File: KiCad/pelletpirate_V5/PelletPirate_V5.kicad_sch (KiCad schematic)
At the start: 130 parts, among them J1 SJ1-3523NG_Jack_PP, J2 SJ1-3523NG_Jack_PP, J3 SJ1-3523NG_Jack_PP, J4 SJ1-3523NG_Jack_PP, J5 SJ1-3523NG_Jack_PP, J6 Conn_01x04, J7 Conn_01x04_Socket, J8 USB4145-03-0170-C, J9 TB002-500-02BE, T1 BTA12-600BWRG, T2 BTA12-600BWRG, T3 BTA12-600BWRG, U1 USBLC6-2SC6, U3 H11AA1M

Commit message: V5 post-cancel fixes: C9 0402, C43 VBUS ballast, C39/C40 boot pair, R20 0805
Order cancelled 2026-08-28; V5 is the active design again. Fixes since:
- C9: footprint corrected to 0402, MPN C0402C104K3RACTU (package now matches part)
- C43 NEW: 100nF 0402 at U1 pin 5, /VBUS->GND ESD ballast (verified 1.63mm from pin)
- C39: EN cap 0.1uF -> 1.0uF 25V KEMET C0603C105K3RACTU (0603 X7R) per Espressif
- C40: IO0 debounce cap rewired +3.3V -> GND (orthodox; linked with C39 change,
  EN delay 10ms >> IO0 rise 1ms, boot-strap race eliminated)
- R20: MPN corrected to RC0805FR-0710KL, footprint normalized to plain 0805
Audits passed on this state: ESP32 pin-by-pin (zero notes), MAX1-5 tiles,
H11AA1/MOC3053, J8/U1 USB, full board-symbol-footprint-BOM reconciliation
(118 refs, 70 package-decoded lines, 0 errors). ERC 0 / DRC 0 / parity 0.

Co-Authored-By: Claude Fable 5 <noreply@anthropic.com>
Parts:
- added C43: 0.1µF 25V, Capacitor_SMD:C_0402_1005Metric, symbol Device:C
- C39: value 0.1µF 25V -> 1.0µF 25V; footprint Capacitor_SMD:C_0402_1005Metric -> Capacitor_SMD:C_0603_1608Metric; LINK https://www.digikey.com/en/products/detail/kemet/C0402C104K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 -> https://www.digikey.com/en/products/detail/kemet/C0603C105K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; MP C0402C104K3RACTU -> C0603C105K3RACTU
- C9: footprint Capacitor_SMD:C_0805_2012Metric -> Capacitor_SMD:C_0402_1005Metric
- R20: footprint Resistor_SMD:R_0805_2012Metric_Pad1.20x1.40mm_HandSolder -> Resistor_SMD:R_0805_2012Metric; LINK https://www.digikey.com/en/products/detail/yageo/RC0402FR-0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 -> https://www.digikey.com/en/products/detail/yageo/RC0805FR-0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; MP RC0402FR-0710KL -> RC0805FR-0710KL
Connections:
- net +3.3V: no longer C40.2
- net GND: now also C40.2, C43.2
- net VBUS: now also C43.1
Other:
- moved on the sheet: C40, C42, R41, R42, R43, TP1, TP2, U3

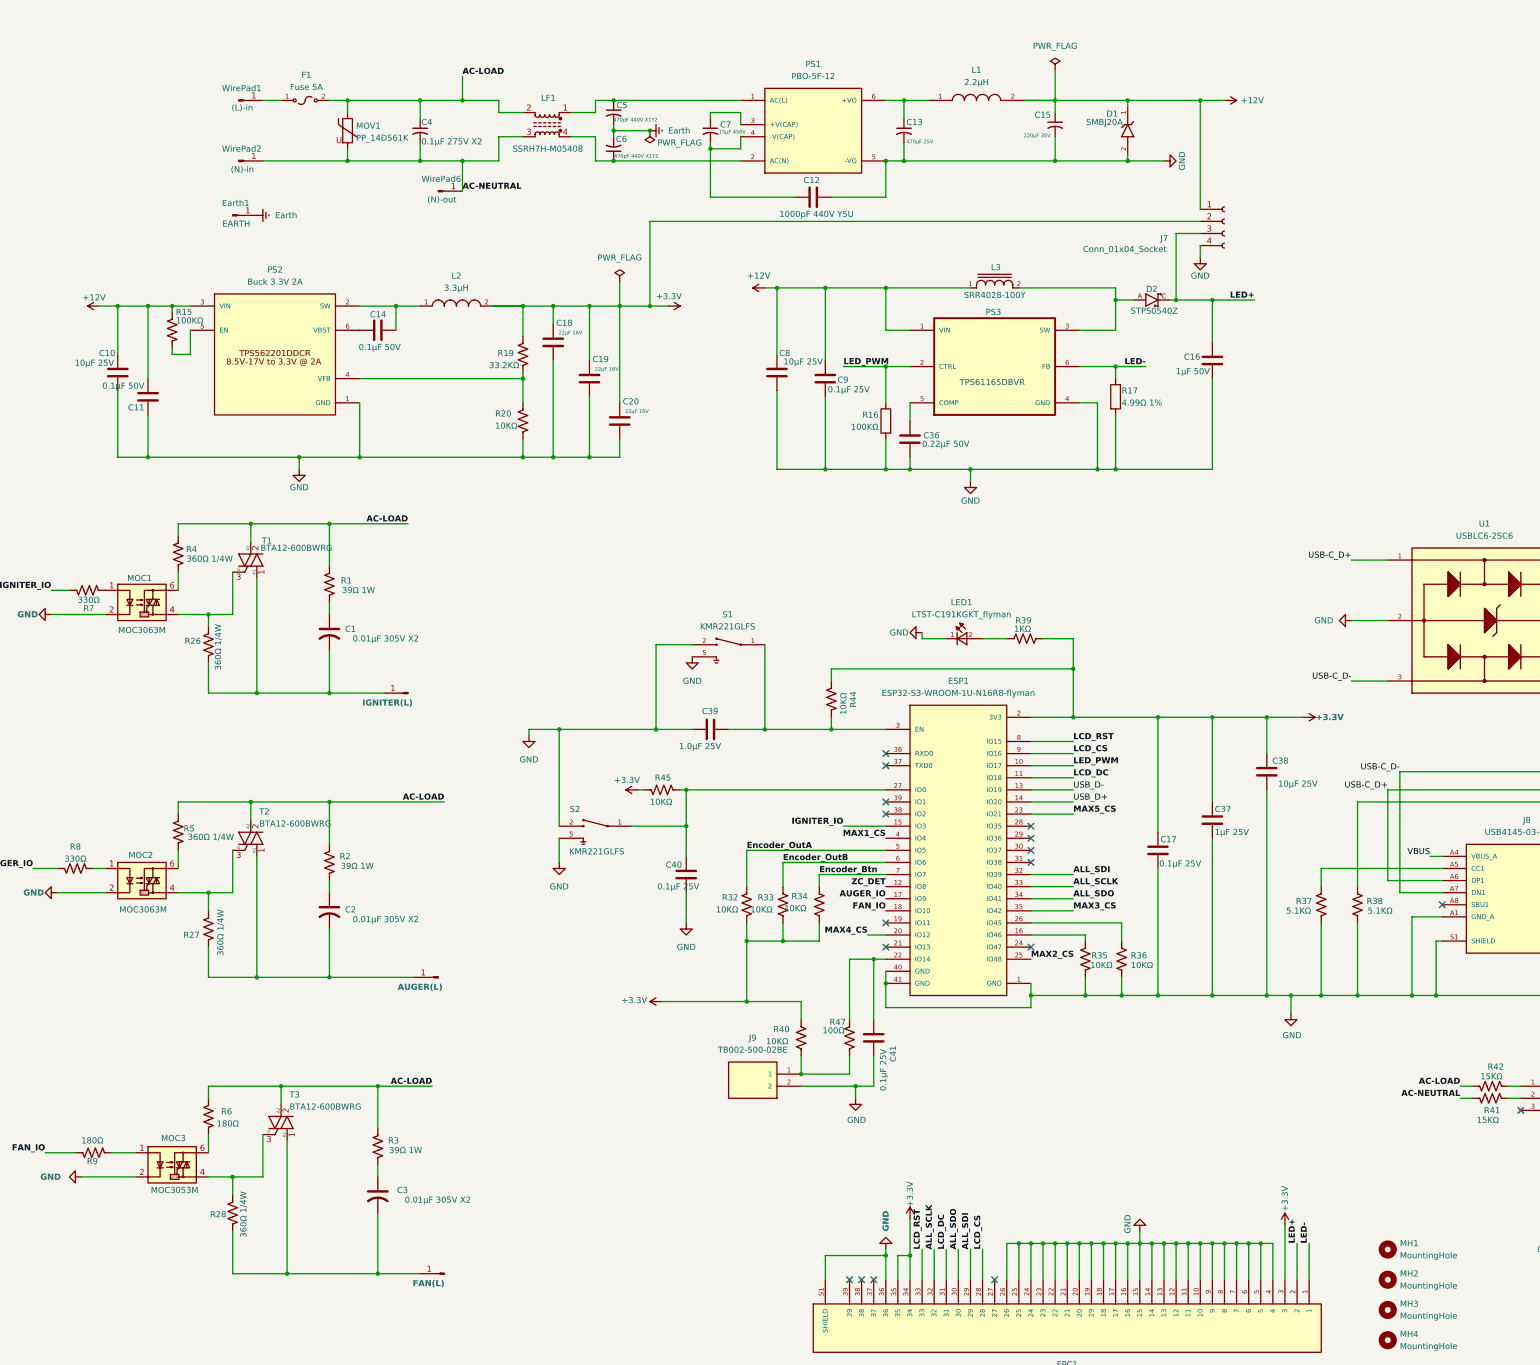
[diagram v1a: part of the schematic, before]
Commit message: V5 raft complete: 4 work packages + C48 damping bulk, all audited, ERC/DRC/netclass clean
WP1: C44/C45 22uF at ESP (raft bulk). WP2: 33R series R at SPI driver pads (R48-51,
stubs <2.2mm). WP3: FL1 bead + C46/C47 panel island (/3V3_LCD, FPC-only membership).
WP4: L5 HF bead after Fig-2 network (D1/C15 upstream preserved) + C48 220uF damping
bulk (resonance 50k->12kHz, Q~1). Netclass patterns added for /3V3_LCD + Net-(C15-Pad1).
EE-soundness review: resonances quantified, Middlebrook margin 80x, timing budgets clear.
Acceptance: runt sentinel 0/min on AC at first article.

Co-Authored-By: Claude Fable 5 <noreply@anthropic.com>
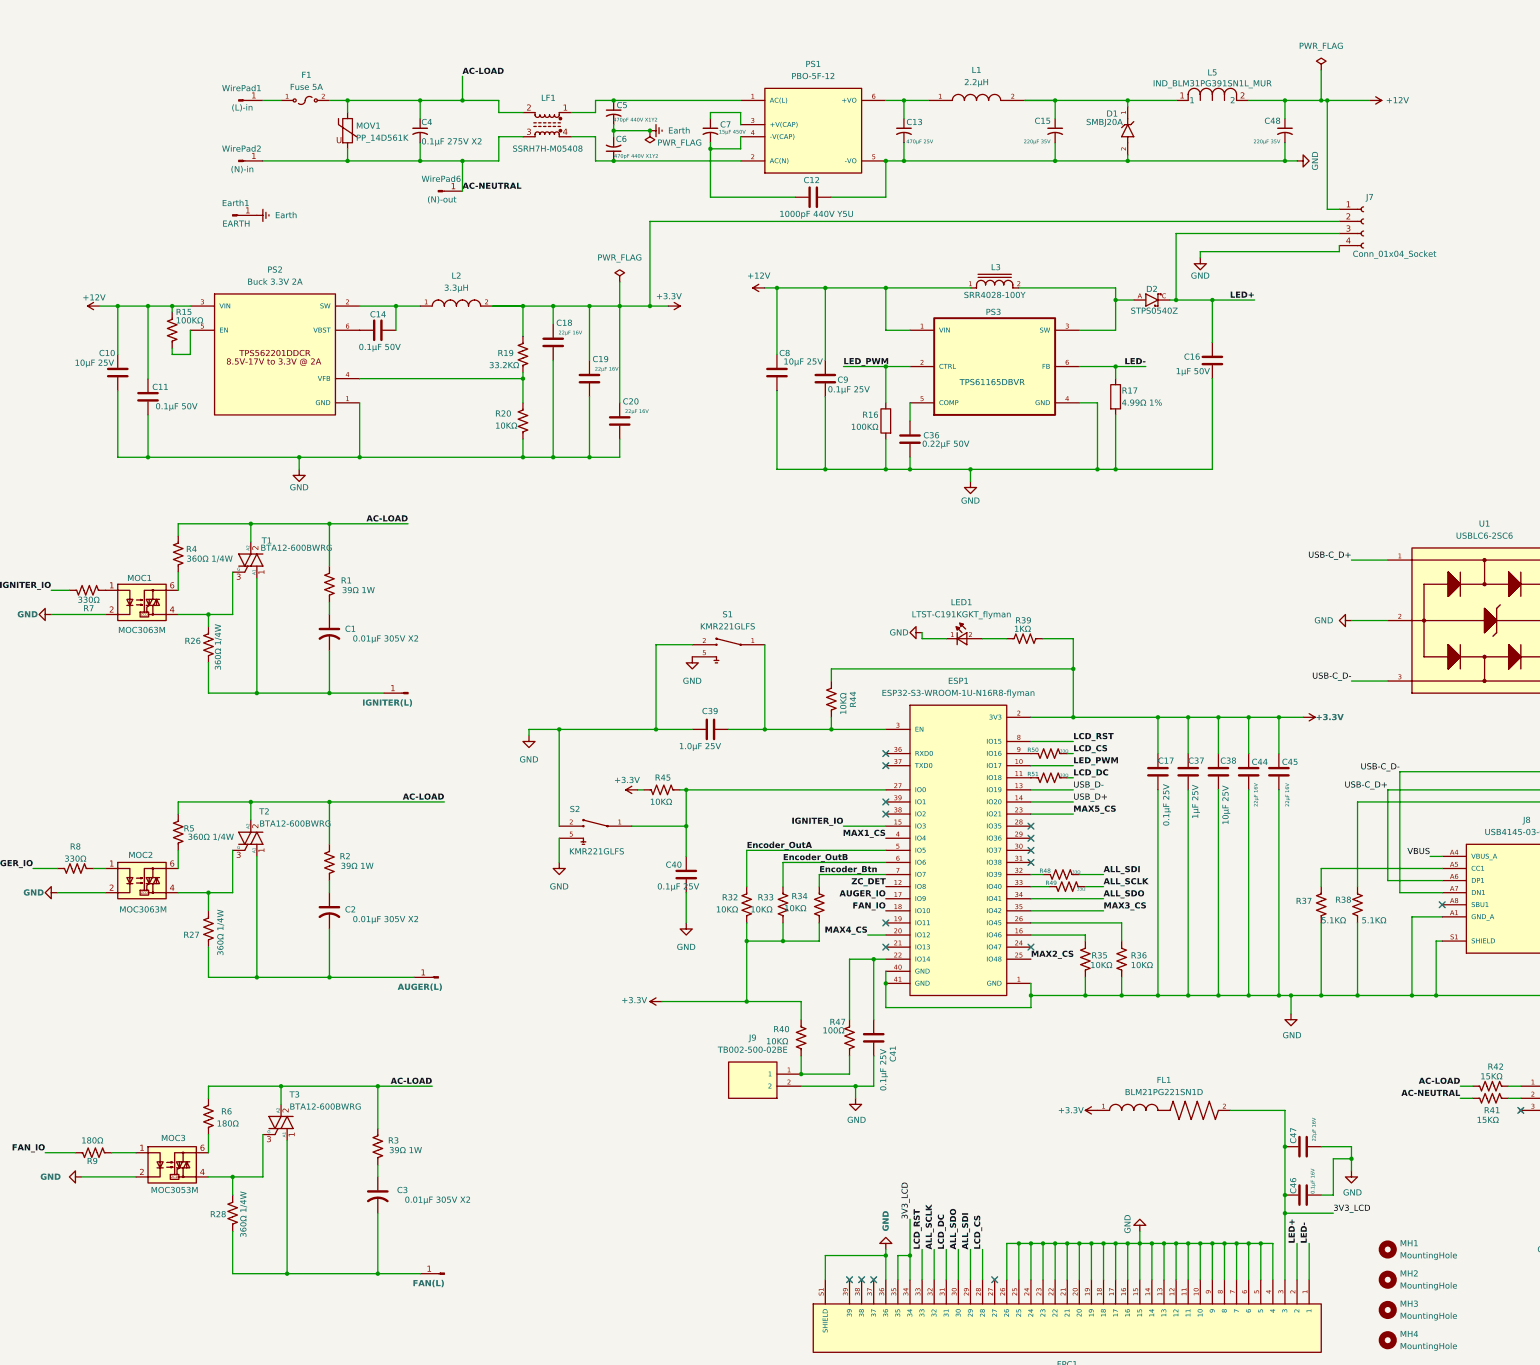
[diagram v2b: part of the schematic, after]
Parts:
- added C44, C45, C47: 22µF 16V, Capacitor_SMD:C_1206_3216Metric, symbol Device:C
- added C46: 0.1µF 16V, Capacitor_SMD:C_0402_1005Metric, symbol Device:C
- added C48: 220µF 35V, Capacitor_THT:CP_Radial_D8.0mm_P3.50mm, symbol Device:C_Small_US
- added FL1: BLM21PG221SN1D, Ferrite_Bead:BEADC2012X105N, symbol BLM21PG221SN1D:BLM21PG221SN1D
- added L5: IND_BLM31PG391SN1L_MUR, Ferrite_Bead_12V:IND_BLM31PG391SN1L_MUR, symbol IND_BLM31PG391SN1L_MUR:IND_BLM31PG391SN1L_MUR
- added R48, R49, R50, R51: 33Ω, Resistor_SMD:R_0402_1005Metric, symbol Device:R_US
- C38: LINK https://www.digikey.com/en/products/detail/kemet/C1206C106K3RACTU/3317648 -> https://www.digikey.com/en/products/detail/kemet/C1206C106K3RACTU/3317648; MP C1206C106K3RACTU -> C1206C106K3RACTU
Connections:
- net +12V: now also C48.1, L5.2; no longer C15.1, D1.1, L1.2
- net +3.3V: now also C44.1, C45.1, FL1.1; no longer FPC1.3, FPC1.34, FPC1.35
- net ALL_SCLK: now also R49.2; no longer ESP1.33 (IO40)
- net ALL_SDI: now also R48.2; no longer ESP1.32 (IO39)
- net GND: now also C44.2, C45.2, C46.1, C47.2, C48.2
- net LCD_CS: now also R50.2; no longer ESP1.9 (IO16)
- net LCD_DC: now also R51.2; no longer ESP1.11 (IO18)
- new net: C15.1, D1.1, L1.2, L5.1
- new net: ESP1.11 (IO18), R51.1
- new net: ESP1.32 (IO39), R48.1
- new net: ESP1.33 (IO40), R49.1
- new net: ESP1.9 (IO16), R50.1
- new net 3V3_LCD: C46.2, C47.1, FL1.2, FPC1.3, FPC1.34, FPC1.35
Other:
- moved on the sheet: C15, C17, C37, C38, J7

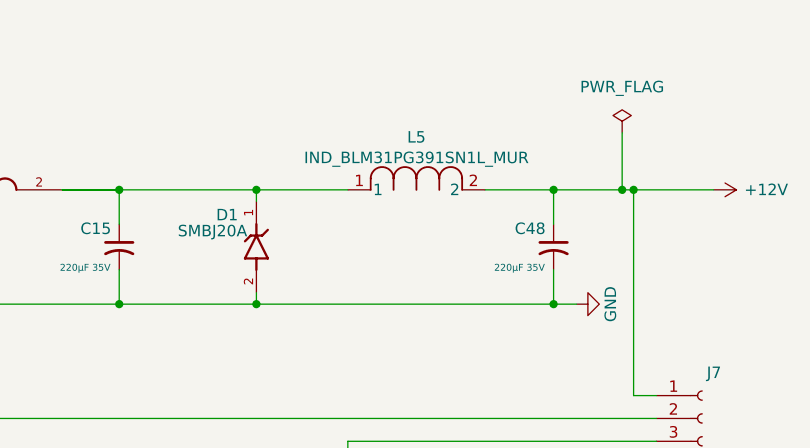
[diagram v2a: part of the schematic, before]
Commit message: V5 PCBWay package regenerated: raft revision, 61 lines / 129 components, 19 no-sub lines
Gerbers+drill (25 slots), positions (148), BOM with FL1/L5/C13/C15+C48 no-sub additions,
assembly notes updated (J9 orientation, C48 polarity, supersedes cancelled 08-27 upload).
Old package archived to archive_to_delete/. L5 601 value+footprint+3D model settled.
J9 flipped: entry faces west edge. Final ERC/DRC 0/0, parity 142/142.

Co-Authored-By: Claude Fable 5 <noreply@anthropic.com>
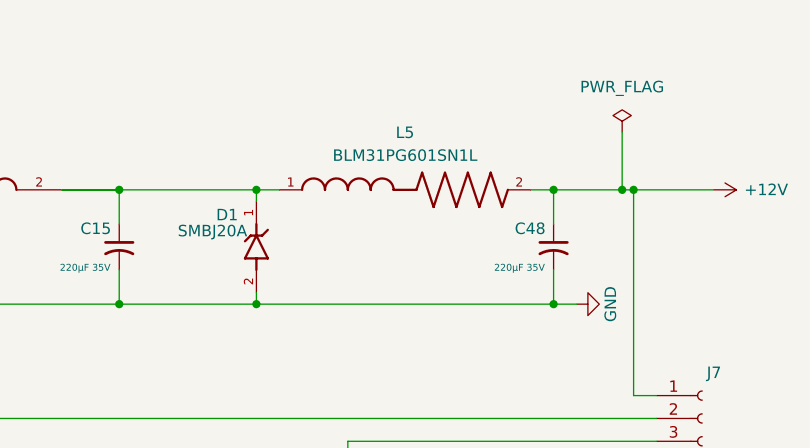
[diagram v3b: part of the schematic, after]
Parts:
- removed L5: IND_BLM31PG391SN1L_MUR, Ferrite_Bead_12V:IND_BLM31PG391SN1L_MUR, symbol IND_BLM31PG391SN1L_MUR:IND_BLM31PG391SN1L_MUR
- added L5: BLM31PG601SN1L, Ferrite_Bead_12V_Flyman:BEADC3216X130N_flyman, symbol BLM31PG601SN1L_flyman:BLM31PG601SN1L
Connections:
- net +12V: now also L5.2
- net at C15.1, D1.1, L1.2: now also L5.1
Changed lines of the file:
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@@
 	)
 	(junction
-		(at 283.21 34.29)
+		(at 452.12 129.54)
 		(diameter 0)
 		(color 0 0 0 0)
 	)
 	(junction
-		(at 452.12 129.54)
+		(at 265.43 274.32)
 		(diameter 0)
 		(color 0 0 0 0)
 	)
 	(junction
-		(at 265.43 274.32)
+		(at 283.21 34.29)
 		(diameter 0)
 		(color 0 0 0 0)
@@
 	(wire
 		(pts
-			(xy 275.59 34.29) (xy 283.21 34.29)
+			(xy 280.67 34.29) (xy 283.21 34.29)
 		)
 		(stroke
@@
 	(wire
 		(pts
-			(xy 250.19 34.29) (xy 260.35 34.29)
+			(xy 250.19 34.29) (xy 252.73 34.29)
 		)
 		(stroke
@@
 	)
 	(symbol
+		(lib_id "BLM31PG601SN1L_flyman:BLM31PG601SN1L")
+		(at 267.97 34.29 0)
+		(unit 1)
+		(body_style 1)
+		(exclude_from_sim no)
+		(in_bom yes)
+		(on_board yes)
+		(in_pos_files yes)
+		(dnp no)
+		(fields_autoplaced yes)
+		(property "Reference" "L5"
+			(at 266.7 27.94 0)
+			(show_name no)
+			(do_not_autoplace no)
+			(effects
+				(font
+					(size 1.27 1.27)
+				)
+			)
+		)
+		(property "Value" "BLM31PG601SN1L"
+			(at 266.7 30.48 0)
+			(show_name no)
+			(do_not_autoplace no)
+			(effects
+				(font
+					(size 1.27 1.27)
+				)
+			)
+		)
+		(property "Footprint" "Ferrite_Bead_12V_Flyman:BEADC3216X130N_flyman"
+			(at 267.97 34.29 0)
+			(hide yes)
+			(show_name no)
+			(do_not_autoplace no)
+			(effects
+				(font
+					(size 1.27 1.27)
+				)
+				(justify bottom)
+			)
+		)
+		(property "Datasheet" ""
+			(at 267.97 34.29 0)
+			(hide yes)
+			(show_name no)
+			(do_not_autoplace no)
+			(effects
+				(font
+					(size 1.27 1.27)
+				)
+			)
+		)
+		(property "Description" "600 Ohms @ 100 MHz 1 Power Line Ferrite Bead 1206 (3216 Metric) 1.5A 80mOhm"
+			(at 267.97 34.29 0)
+			(hide yes)
+			(show_name no)
+			(do_not_autoplace no)
+			(effects
+				(font
+					(size 1.27 1.27)
+				)
+				(justify bottom)
+			)
+		)
+		(property "MF" "Murata"
+			(at 267.97 34.29 0)
+			(hide yes)
+			(show_name no)
+			(do_not_autoplace no)
+			(effects
+				(font
+					(size 1.27 1.27)
+				)
+				(justify bottom)
+			)
+		)
+		(property "Package" "3216 Murata"
+			(at 267.97 34.29 0)
+			(hide yes)
+			(show_name no)
+			(do_not_autoplace no)
+			(effects
+				(font
+					(size 1.27 1.27)
+				)
+				(justify bottom)
+			)
+		)
+		(property "Price" "None"
+			(at 267.97 34.29 0)
+			(hide yes)
+			(show_name no)
+			(do_not_autoplace no)
+			(effects
+				(font
+					(size 1.27 1.27)
+				)
+				(justify bottom)
+			)
+		)
+		(property "SnapEDA_Link" "https://www.snapeda.com/parts/BLM31PG601SN1L/Murata/view-part/?ref=snap"
+			(at 267.97 34.29 0)
+			(hide yes)
+			(show_name no)
+			(do_not_autoplace no)
+			(effects
+				(font
+					(size 1.27 1.27)
+				)
+				(justify bottom)
+			)
+		)
+		(property "MP" "BLM31PG601SN1L"
+			(at 267.97 34.29 0)
+			(hide yes)
+			(show_name no)
+			(do_not_autoplace no)
+			(effects
+				(font
+					(size 1.27 1.27)
+				)
+				(justify bottom)
+			)
+		)
+		(property "Availability" "In Stock"
+			(at 267.97 34.29 0)
+			(hide yes)
+			(show_name no)
+			(do_not_autoplace no)
+			(effects
+				(font
+					(size 1.27 1.27)
+				)
+				(justify bottom)
+			)
+		)
+		(property "Check_prices" "https://www.snapeda.com/parts/BLM31PG601SN1L/Murata/view-part/?ref=eda"
+			(at 267.97 34.29 0)
+			(hide yes)
+			(show_name no)
+			(do_not_autoplace no)
+			(effects
+				(font
+					(size 1.27 1.27)
+				)
+				(justify bottom)
+			)
+		)
+		(pin "2"
+		)
+		(pin "1"
+		)
+		(instances
+			(project "PelletPirate_V5"
+				(path "/0182ac56-03c6-4c14-8ead-12e31828f094"
+					(reference "L5")
+					(unit 1)
+				)
+			)
+		)
+	)
+	(symbol
 		(lib_id "Device:R_US")
 		(at 237.49 199.39 90)
@@
 					(unit 1)
 				)
-			)
-		)
-	)
-	(symbol
-		(lib_id "IND_BLM31PG391SN1L_MUR:IND_BLM31PG391SN1L_MUR")
-		(at 275.59 34.29 0)
-		(mirror y)
-		(unit 1)
-		(body_style 1)
-		(exclude_from_sim no)
-		(in_bom yes)
-		(on_board yes)
-		(in_pos_files yes)
-		(dnp no)
-		(property "Reference" "L5"
-			(at 267.97 28.448 0)
-			(show_name no)
-			(do_not_autoplace no)
-			(effects
-				(font
-					(size 1.27 1.27)
-				)
-			)
-		)
-		(property "Value" "IND_BLM31PG391SN1L_MUR"
-			(at 267.97 30.734 0)
-			(show_name no)
-			(do_not_autoplace no)
-			(effects
-				(font
-					(size 1.27 1.27)
-				)
-			)
-		)
-		(property "Footprint" "Ferrite_Bead_12V:IND_BLM31PG391SN1L_MUR"
-			(at 275.59 34.29 0)
-			(hide yes)
-			(show_name no)
-			(do_not_autoplace no)
-			(effects
-				(font
-					(size 1.27 1.27)
-					(italic yes)
-				)
-			)
-		)
-		(property "Datasheet" "BLM31PG601SN1L"
-			(at 275.59 34.29 0)
-			(hide yes)
-			(show_name no)
-			(do_not_autoplace no)
-			(effects
-				(font
-					(size 1.27 1.27)
-					(italic yes)
-				)
-			)
-		)
-		(property "Description" "FERRITE BEAD 600 OHM 1206 1LN"
-			(at 275.59 34.29 0)
-			(hide yes)
-			(show_name no)
-			(do_not_autoplace no)
-			(effects
-				(font
-					(size 1.27 1.27)
-				)
-			)
-		)
-		(property "LINK" "https://www.digikey.com/en/products/detail/murata-electronics/BLM31PG601SN1L/584266"
-			(at 275.59 34.29 0)
-			(hide yes)
-			(show_name no)
-			(do_not_autoplace no)
-			(effects
-				(font
-					(size 1.27 1.27)
-				)
-			)
-		)
-		(property "MF" "Murata"
-			(at 275.59 34.29 0)
-			(hide yes)
-			(show_name no)
-			(do_not_autoplace no)
-			(effects
-				(font
-					(size 1.27 1.27)
-				)
-			)
-		)
-		(property "MP" "BLM31PG601SN1L"
-			(at 275.59 34.29 0)
-			(hide yes)
-			(show_name no)
-			(do_not_autoplace no)
-			(effects
-				(font
-					(size 1.27 1.27)
-				)
-			)
-		)
-		(pin "1"
-		)
-		(pin "2"
-		)
-		(instances
-			(project "PelletPirate_V5"
-				(path "/0182ac56-03c6-4c14-8ead-12e31828f094"
-					(reference "L5")
-					(unit 1)
-				)
